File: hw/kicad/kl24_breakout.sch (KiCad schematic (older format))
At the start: 53 parts, among them J1 USB-micro-ab, P1 TST, P10 TST, P11 TST, P12 TST, P13 TST, P14 TST, P15 TST, P16 TST, P17 TST, P18 TST, P19 TST, P2 TST, P20 TST, P21 TST, P22 TST, P23 TST, P24 TST, P25 TST, P26 TST, P27 TST, P28 TST, P29 TST, P3 TST, P30 TST, P31 TST, P32 TST, P33 USB_V, P34 USB_GND, P35 SWD_VCC, P36 SWDIO, P37 SWCLK, P38 NRESET, P39 SWD_GND, P4 TST, P5 TST, P6 TST, P7 TST, P8 TST, P9 TST, U1 MKL24Z64VFM4, U2 LP3985, X1 CRYSTAL

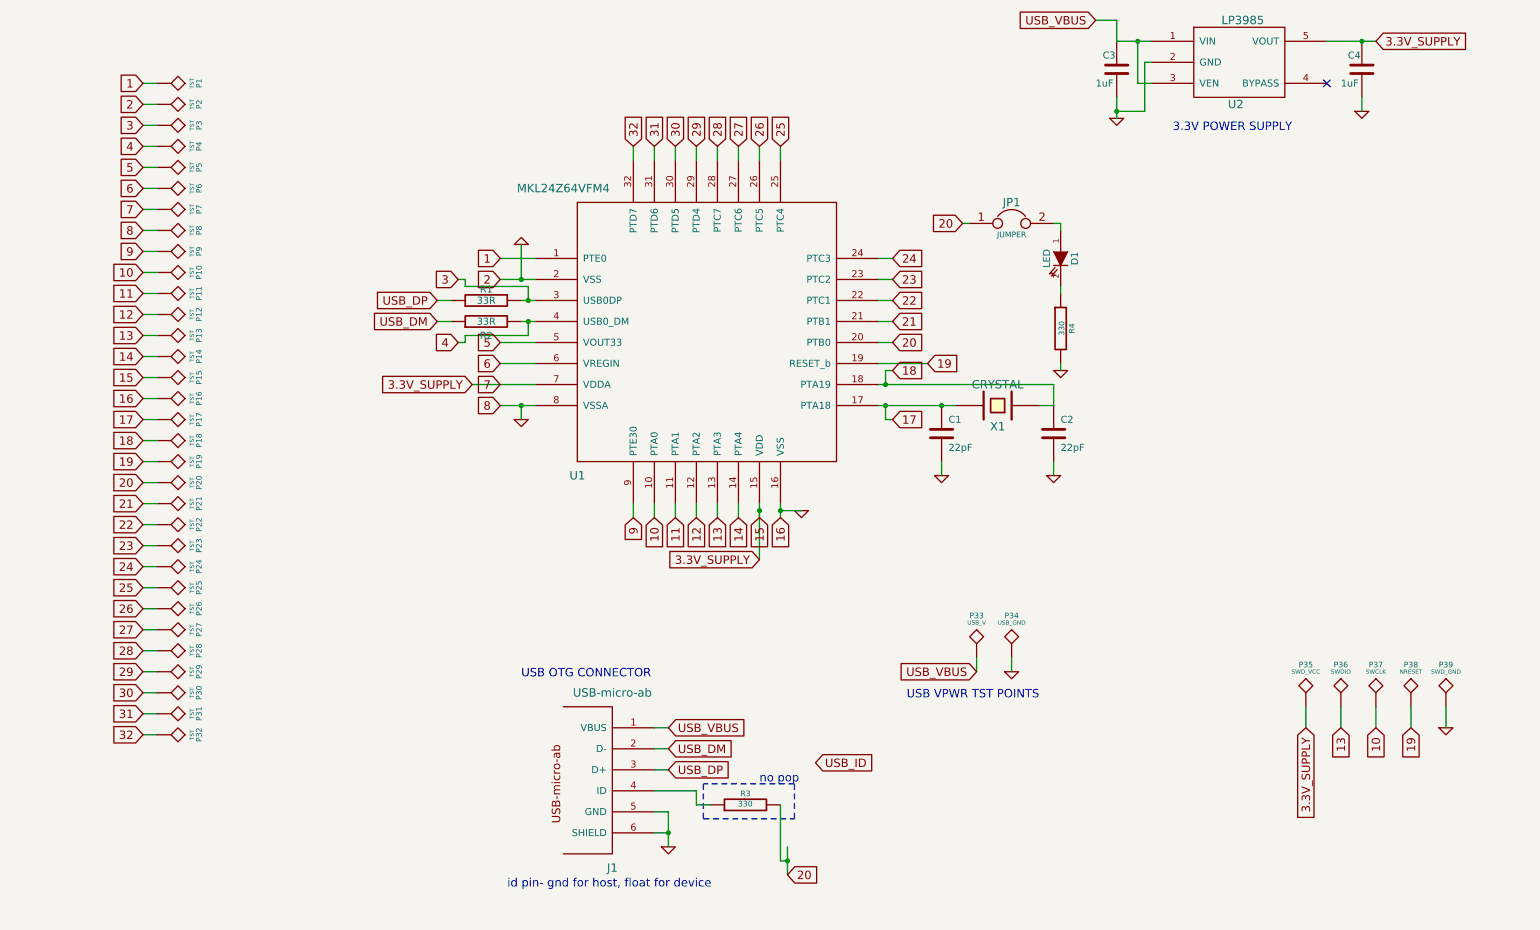
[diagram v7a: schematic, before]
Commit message: remove regulator in favor of on-chip 3.3v regulator
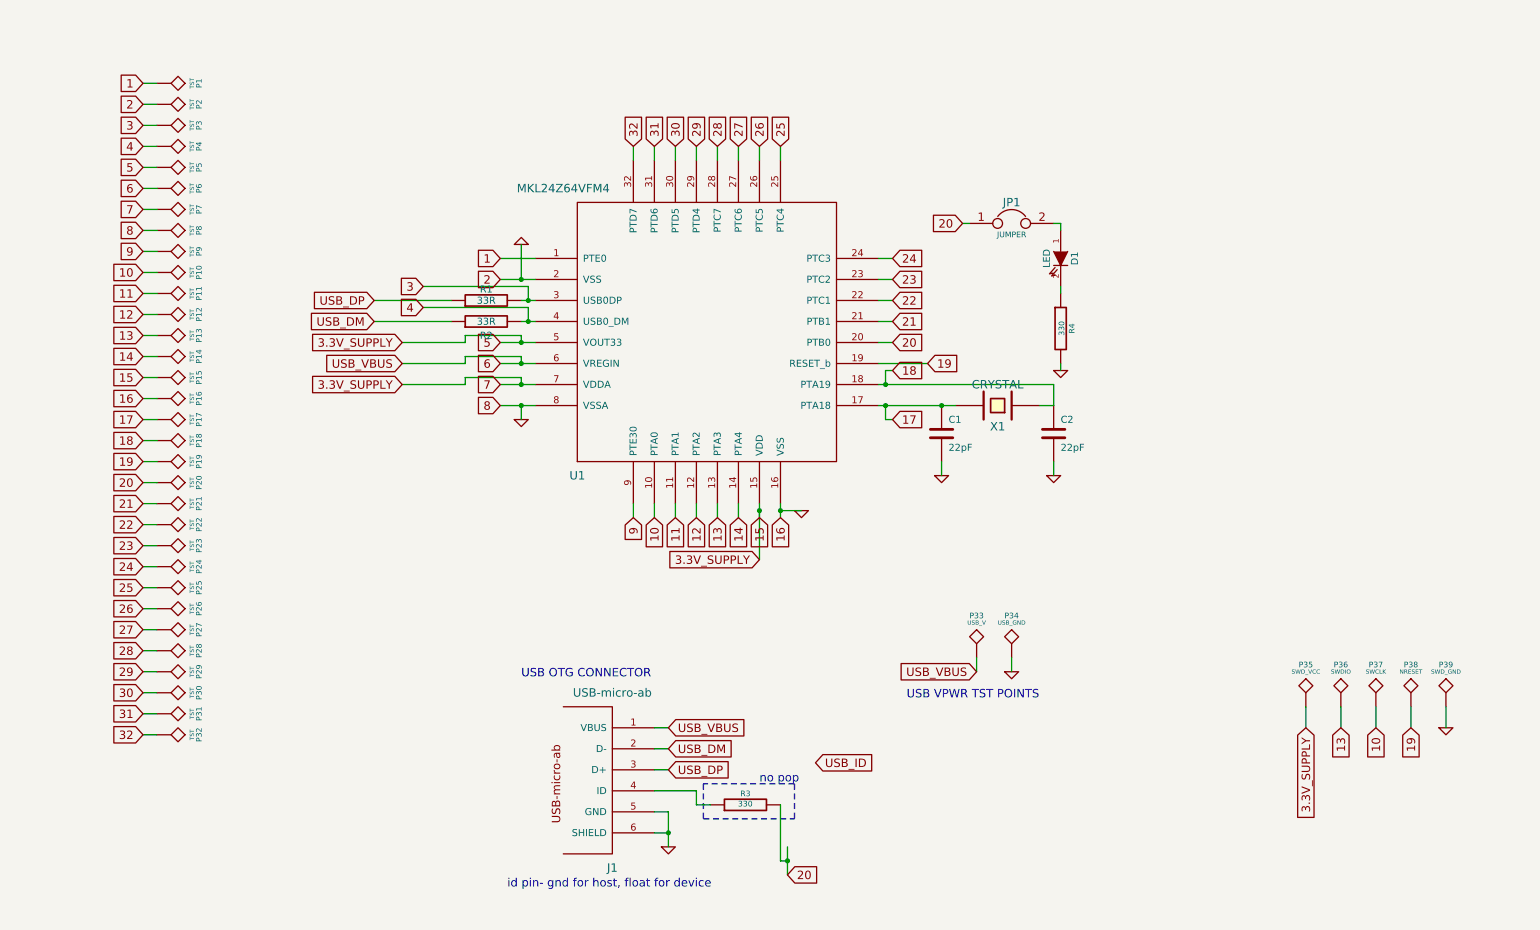
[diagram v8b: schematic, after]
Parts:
- removed C3, C4: 1uF, symbol C
- removed U2: LP3985, symbol LP3985
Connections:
- net 5 is gone; now on net 15: P5.1, U1.5 (VOUT33)
- net USB_VBUS is gone; now on net 6: J1.1 (VBUS), P33.1
- no-connect marks 1 -> 0
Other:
- note removed: "3.3V POWER SUPPLY"
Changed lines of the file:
@@
-EESchema Schematic File Version 2
+EESchema Schematic File Version 2  date 10/14/2013 1:18:17 PM
 LIBS:power
 LIBS:device
@@
 Sheet 1 1
 Title ""
-Date "13 oct 2013"
+Date "14 oct 2013"
 Rev ""
 Comp ""
@@
 $EndDescr
 Wire Wire Line
-	8400 850  8400 1150
-Wire Wire Line
 	1300 5800 1400 5800
 Wire Wire Line
@@
 Wire Wire Line
 	4000 3450 4000 3550
-Connection ~ 10000 850
-Wire Wire Line
-	10000 1250 10000 1350
-Wire Wire Line
-	9750 850  10100 850
-Connection ~ 8250 1350
-Wire Wire Line
-	8250 1250 8250 1400
-Wire Wire Line
-	8250 1350 8450 1350
-Wire Wire Line
-	8450 1350 8450 1000
-Wire Wire Line
-	8450 1000 8500 1000
-Wire Wire Line
-	8400 1150 8500 1150
 Wire Wire Line
 	5850 1600 5850 1700
@@
 	3850 3450 4100 3450
 Wire Wire Line
-	3650 3300 4100 3300
-Wire Wire Line
-	3850 3150 4100 3150
-Wire Wire Line
-	3850 3000 4100 3000
-Connection ~ 4050 2850
-Wire Wire Line
-	4050 2850 4050 2950
-Wire Wire Line
-	4050 2950 3600 2950
-Wire Wire Line
-	3600 2950 3600 3000
-Wire Wire Line
-	3600 3000 3550 3000
-Connection ~ 4050 2700
-Wire Wire Line
-	4050 2700 4050 2600
-Wire Wire Line
-	4050 2600 3600 2600
-Wire Wire Line
-	3600 2600 3600 2550
-Wire Wire Line
-	3600 2550 3550 2550
-Wire Wire Line
 	3850 2550 4100 2550
 Wire Wire Line
 	3850 2400 4100 2400
-Wire Wire Line
-	3500 2700 3400 2700
-Wire Wire Line
-	4000 2700 4100 2700
-Wire Wire Line
-	4000 2850 4100 2850
-Wire Wire Line
-	3400 2850 3500 2850
 Wire Wire Line
 	7800 3450 7700 3450
@@
 $EndComp
 $Comp
-L LP3985 U2
-U 1 1 513635E4
-P 9100 1000
-F 0 "U2" H 9100 700 60  0000 C CNN
-F 1 "LP3985" H 9150 1300 60  0000 C CNN
-F 2 "" H 9100 1000 60  0001 C CNN
-F 3 "" H 9100 1000 60  0001 C CNN
-	1    9100 1000
-	1    0    0    -1
-$EndComp
-$Comp
 L USB-micro-ab J1
 U 1 1 5135355A
@@
 	1    0    0    -1
 $EndComp
-Text GLabel 3400 2850 0    60   Input ~ 0
+Text GLabel 2950 2850 0    60   Input ~ 0
 USB_DM
 $Comp
@@
 	0    -1   -1   0
 $EndComp
-Text GLabel 3400 2700 0    60   Input ~ 0
+Text GLabel 2950 2700 0    60   Input ~ 0
 USB_DP
 $Comp
@@
 Text GLabel 3850 2550 0    60   Input ~ 0
 2
-Text GLabel 3550 2550 0    60   Input ~ 0
+Text GLabel 3300 2600 0    60   Input ~ 0
 3
-Text GLabel 3550 3000 0    60   Input ~ 0
+Text GLabel 3300 2750 0    60   Input ~ 0
 4
 Text GLabel 3850 3000 0    60   Input ~ 0
@@
 Text Notes 4000 5400 0    60   ~ 0
 USB OTG CONNECTOR
-Text Notes 8650 1500 0    60   ~ 0
-3.3V POWER SUPPLY
 Text GLabel 10100 5750 3    60   Input ~ 0
 10
@@
 	1    0    0    -1
 $EndComp
-$Comp
-L C C3
-U 1 1 513F995C
-P 8250 1050
-F 0 "C3" H 8150 1150 50  0000 L CNN
-F 1 "1uF" H 8100 950 50  0000 L CNN
-F 2 "" H 8250 1050 60  0001 C CNN
-F 3 "" H 8250 1050 60  0001 C CNN
-	1    8250 1050
-	1    0    0    -1
-$EndComp
-$Comp
-L C C4
-U 1 1 513F9967
-P 10000 1050
-F 0 "C4" H 9900 1150 50  0000 L CNN
-F 1 "1uF" H 9850 950 50  0000 L CNN
-F 2 "" H 10000 1050 60  0001 C CNN
-F 3 "" H 10000 1050 60  0001 C CNN
-	1    10000 1050
-	1    0    0    -1
-$EndComp
+Text GLabel 3150 3300 0    60   Input ~ 0
+3.3V_SUPPLY
 $Comp
 L GND #PWR05
-U 1 1 513F9B6C
-P 8250 1400
-F 0 "#PWR05" H 8250 1400 30  0001 C CNN
-F 1 "GND" H 8250 1330 30  0001 C CNN
-F 2 "" H 8250 1400 60  0001 C CNN
-F 3 "" H 8250 1400 60  0001 C CNN
-	1    8250 1400
-	1    0    0    -1
-$EndComp
-$Comp
-L GND #PWR06
-U 1 1 513F9C7F
-P 10000 1350
-F 0 "#PWR06" H 10000 1350 30  0001 C CNN
-F 1 "GND" H 10000 1280 30  0001 C CNN
-F 2 "" H 10000 1350 60  0001 C CNN
-F 3 "" H 10000 1350 60  0001 C CNN
-	1    10000 1350
-	1    0    0    -1
-$EndComp
-Text GLabel 10100 850  2    60   Input ~ 0
-3.3V_SUPPLY
-Text GLabel 3650 3300 0    60   Input ~ 0
-3.3V_SUPPLY
-$Comp
-L GND #PWR07
 U 1 1 513FA04E
 P 4000 3550
-F 0 "#PWR07" H 4000 3550 30  0001 C CNN
+F 0 "#PWR05" H 4000 3550 30  0001 C CNN
 F 1 "GND" H 4000 3480 30  0001 C CNN
 F 2 "" H 4000 3550 60  0001 C CNN
@@
 $EndComp
 $Comp
-L GND #PWR08
+L GND #PWR06
 U 1 1 513FA1BA
 P 4000 2300
-F 0 "#PWR08" H 4000 2300 30  0001 C CNN
+F 0 "#PWR06" H 4000 2300 30  0001 C CNN
 F 1 "GND" H 4000 2230 30  0001 C CNN
 F 2 "" H 4000 2300 60  0001 C CNN
@@
 	-1   0    0    1
 $EndComp
-NoConn ~ 9750 1150
 $Comp
 L TST P1
@@
 	7250 5350 7250 5250
 $Comp
-L GND #PWR09
+L GND #PWR07
 U 1 1 5169787E
 P 7500 5350
-F 0 "#PWR09" H 7500 5350 30  0001 C CNN
+F 0 "#PWR07" H 7500 5350 30  0001 C CNN
 F 1 "GND" H 7500 5280 30  0001 C CNN
 F 2 "" H 7500 5350 60  0001 C CNN
@@
 $EndComp
 $Comp
-L GND #PWR010
+L GND #PWR08
 U 1 1 519F5DBB
 P 7850 3200
-F 0 "#PWR010" H 7850 3200 30  0001 C CNN
+F 0 "#PWR08" H 7850 3200 30  0001 C CNN
 F 1 "GND" H 7850 3130 30  0001 C CNN
 F 2 "" H 7850 3200 60  0001 C CNN
@@
 Wire Wire Line
 	7850 2150 7850 2200
-Text GLabel 8100 700  0    60   Input ~ 0
-USB_VBUS
-Wire Wire Line
-	8250 850  8500 850
-Connection ~ 8400 850
-Wire Wire Line
-	8100 700  8250 700
-Wire Wire Line
-	8250 700  8250 850
 Text GLabel 5900 6800 2    60   Input ~ 0
 20
@@
 no pop
 $Comp
-L GND #PWR011
+L GND #PWR09
 U 1 1 525B1F5C
 P 6000 4200
-F 0 "#PWR011" H 6000 4200 30  0001 C CNN
+F 0 "#PWR09" H 6000 4200 30  0001 C CNN
 F 1 "GND" H 6000 4130 30  0001 C CNN
 F 2 "" H 6000 4200 60  0001 C CNN
@@
 	5700 4200 5700 4550
 Connection ~ 5700 4200
+Text GLabel 3150 3150 0    60   Input ~ 0
+USB_VBUS
+Text GLabel 3150 3000 0    60   Input ~ 0
+3.3V_SUPPLY
+Wire Wire Line
+	4100 2850 4000 2850
+Wire Wire Line
+	4050 2850 4050 2750
+Wire Wire Line
+	4050 2750 3300 2750
+Connection ~ 4050 2850
+Wire Wire Line
+	3500 2850 2950 2850
+Wire Wire Line
+	2950 2700 3500 2700
+Wire Wire Line
+	4100 2700 4000 2700
+Wire Wire Line
+	4050 2700 4050 2600
+Wire Wire Line
+	4050 2600 3300 2600
+Connection ~ 4050 2700
+Wire Wire Line
+	3850 3000 4100 3000
+Wire Wire Line
+	3150 3000 3600 3000
+Wire Wire Line
+	3600 3000 3600 2950
+Wire Wire Line
+	3600 2950 4000 2950
+Wire Wire Line
+	4000 2950 4000 3000
+Connection ~ 4000 3000
+Wire Wire Line
+	4100 3150 3850 3150
+Wire Wire Line
+	3850 3300 4100 3300
+Wire Wire Line
+	4000 3150 4000 3100
+Wire Wire Line
+	4000 3100 3600 3100
+Wire Wire Line
+	3600 3100 3600 3150
+Wire Wire Line
+	3600 3150 3150 3150
+Connection ~ 4000 3150
+Wire Wire Line
+	3150 3300 3600 3300
+Wire Wire Line
+	3600 3300 3600 3250
+Wire Wire Line
+	3600 3250 4000 3250
+Wire Wire Line
+	4000 3250 4000 3300
+Connection ~ 4000 3300
 $EndSCHEMATC
